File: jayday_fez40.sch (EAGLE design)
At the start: 46 parts, among them IC1 GHI_STM32F40X, IC2 LM1117MP-3.3, IC9 MIC4680-ADJ, U3 MICROSD_MICROSD, X4 DX2R005HN2E700

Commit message: finished layout
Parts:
- renumbered N_M_SENS to M_SENS, P+12V to +12V, P+5V to +5V, P+VCC to VCC, X_LCD_OUT to LCD_OUT
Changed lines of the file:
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@@
 <part name="SUPPLY8" library="supply2" deviceset="+5V" device=""/>
 <part name="U$2" library="SparkFun-Connectors" deviceset="RJ45-8" device="PTH"/>
-<part name="X_LCD_OUT" library="ozlollc" deviceset="SHF105" device=""/>
+<part name="LCD_OUT" library="ozlollc" deviceset="SHF105" device=""/>
 <part name="N_M_HEAT" library="ozlollc" deviceset="SI2312BDS" device=""/>
-<part name="N_M_SENS" library="ozlollc" deviceset="SI2312BDS" device=""/>
+<part name="M_SENS" library="ozlollc" deviceset="SI2312BDS" device=""/>
 <part name="SIM900-EXT" library="SparkFun-Connectors" deviceset="M08" device="1X08"/>
 <part name="GND3" library="supply1" deviceset="GND" device=""/>
 <part name="SUPPLY9" library="supply2" deviceset="+12V" device=""/>
 <part name="GND7" library="supply1" deviceset="GND" device=""/>
-<part name="P+5V" library="led" deviceset="LED" device="CHIPLED_0805"/>
+<part name="+5V" library="led" deviceset="LED" device="CHIPLED_0805"/>
 <part name="R7" library="rcl" deviceset="R-US_" device="R0603" value="330"/>
 <part name="V1" library="supply2" deviceset="+5V" device=""/>
 <part name="GND10" library="supply1" deviceset="GND" device=""/>
-<part name="P+VCC" library="led" deviceset="LED" device="CHIPLED_0805"/>
+<part name="VCC" library="led" deviceset="LED" device="CHIPLED_0805"/>
 <part name="R8" library="rcl" deviceset="R-US_" device="R0603" value="330"/>
 <part name="GND11" library="supply1" deviceset="GND" device=""/>
-<part name="P+12V" library="led" deviceset="LED" device="CHIPLED_0805"/>
+<part name="+12V" library="led" deviceset="LED" device="CHIPLED_0805"/>
 <part name="R9" library="rcl" deviceset="R-US_" device="R0603" value="330"/>
 <part name="SUPPLY10" library="supply2" deviceset="+12V" device=""/>
@@
 <instance part="SUPPLY8" gate="+5V" x="111.76" y="116.84" rot="R180"/>
 <instance part="U$2" gate="G$1" x="162.56" y="124.46"/>
-<instance part="X_LCD_OUT" gate="X" x="22.86" y="104.14"/>
+<instance part="LCD_OUT" gate="X" x="22.86" y="104.14"/>
 <instance part="N_M_HEAT" gate="G$1" x="106.68" y="165.1"/>
-<instance part="N_M_SENS" gate="G$1" x="187.96" y="165.1"/>
+<instance part="M_SENS" gate="G$1" x="187.96" y="165.1"/>
 <instance part="SIM900-EXT" gate="G$1" x="243.84" y="121.92"/>
 <instance part="GND3" gate="1" x="261.62" y="106.68"/>
 <instance part="SUPPLY9" gate="+12V" x="256.54" y="106.68" rot="R180"/>
 <instance part="GND7" gate="1" x="203.2" y="-17.78"/>
-<instance part="P+5V" gate="G$1" x="203.2" y="-7.62"/>
+<instance part="+5V" gate="G$1" x="203.2" y="-7.62"/>
 <instance part="R7" gate="G$1" x="203.2" y="2.54" rot="R90"/>
 <instance part="V1" gate="+5V" x="203.2" y="12.7"/>
 <instance part="GND10" gate="1" x="213.36" y="-17.78"/>
-<instance part="P+VCC" gate="G$1" x="213.36" y="-7.62"/>
+<instance part="VCC" gate="G$1" x="213.36" y="-7.62"/>
 <instance part="R8" gate="G$1" x="213.36" y="2.54" rot="R90"/>
 <instance part="GND11" gate="1" x="193.04" y="-17.78"/>
-<instance part="P+12V" gate="G$1" x="193.04" y="-7.62"/>
+<instance part="+12V" gate="G$1" x="193.04" y="-7.62"/>
 <instance part="R9" gate="G$1" x="193.04" y="2.54" rot="R90"/>
 <instance part="SUPPLY10" gate="+12V" x="193.04" y="12.7"/>
@@
 </segment>
 <segment>
-<pinref part="P+5V" gate="G$1" pin="C"/>
+<pinref part="+5V" gate="G$1" pin="C"/>
 <pinref part="GND7" gate="1" pin="GND"/>
 <wire x1="203.2" y1="-12.7" x2="203.2" y2="-15.24" width="0.1524" layer="91"/>
 </segment>
 <segment>
-<pinref part="P+VCC" gate="G$1" pin="C"/>
+<pinref part="VCC" gate="G$1" pin="C"/>
 <pinref part="GND10" gate="1" pin="GND"/>
 <wire x1="213.36" y1="-12.7" x2="213.36" y2="-15.24" width="0.1524" layer="91"/>
 </segment>
 <segment>
-<pinref part="P+12V" gate="G$1" pin="C"/>
+<pinref part="+12V" gate="G$1" pin="C"/>
 <pinref part="GND11" gate="1" pin="GND"/>
 <wire x1="193.04" y1="-12.7" x2="193.04" y2="-15.24" width="0.1524" layer="91"/>
@@
 <wire x1="185.42" y1="149.86" x2="187.96" y2="149.86" width="0.1524" layer="91"/>
 <junction x="187.96" y="149.86"/>
-<pinref part="N_M_SENS" gate="G$1" pin="S"/>
+<pinref part="M_SENS" gate="G$1" pin="S"/>
 <pinref part="R11" gate="G$1" pin="1"/>
 <wire x1="172.72" y1="152.4" x2="172.72" y2="149.86" width="0.1524" layer="91"/>
@@
 <segment>
 <pinref part="SUPPLY15" gate="G$1" pin="VCC"/>
-<pinref part="X_LCD_OUT" gate="X" pin="1"/>
+<pinref part="LCD_OUT" gate="X" pin="1"/>
 </segment>
 <segment>
@@
 </segment>
 <segment>
-<pinref part="X_LCD_OUT" gate="X" pin="2"/>
+<pinref part="LCD_OUT" gate="X" pin="2"/>
 <pinref part="SUPPLY13" gate="+5V" pin="+5V"/>
 </segment>
@@
 </segment>
 <segment>
-<pinref part="X_LCD_OUT" gate="X" pin="6"/>
+<pinref part="LCD_OUT" gate="X" pin="6"/>
 <wire x1="33.02" y1="104.14" x2="58.42" y2="104.14" width="0.1524" layer="91"/>
 <label x="35.56" y="104.14" size="1.778" layer="95"/>
@@
 </segment>
 <segment>
-<pinref part="X_LCD_OUT" gate="X" pin="8"/>
+<pinref part="LCD_OUT" gate="X" pin="8"/>
 <wire x1="33.02" y1="101.6" x2="55.88" y2="101.6" width="0.1524" layer="91"/>
 <wire x1="55.88" y1="101.6" x2="58.42" y2="101.6" width="0.1524" layer="91"/>
@@
 </segment>
 <segment>
-<pinref part="X_LCD_OUT" gate="X" pin="7"/>
+<pinref part="LCD_OUT" gate="X" pin="7"/>
 <wire x1="12.7" y1="101.6" x2="-17.78" y2="101.6" width="0.1524" layer="91"/>
 <label x="-22.86" y="101.6" size="1.778" layer="95"/>
@@
 </segment>
 <segment>
-<pinref part="X_LCD_OUT" gate="X" pin="9"/>
+<pinref part="LCD_OUT" gate="X" pin="9"/>
 <wire x1="12.7" y1="99.06" x2="-17.78" y2="99.06" width="0.1524" layer="91"/>
 <label x="-22.86" y="99.06" size="1.778" layer="95"/>
@@
 </segment>
 <segment>
-<pinref part="X_LCD_OUT" gate="X" pin="5"/>
+<pinref part="LCD_OUT" gate="X" pin="5"/>
 <wire x1="12.7" y1="104.14" x2="-17.78" y2="104.14" width="0.1524" layer="91"/>
 <label x="-22.86" y="104.14" size="1.778" layer="95"/>
@@
 </segment>
 <segment>
-<pinref part="N_M_SENS" gate="G$1" pin="G"/>
+<pinref part="M_SENS" gate="G$1" pin="G"/>
 <wire x1="182.88" y1="162.56" x2="172.72" y2="162.56" width="0.1524" layer="91"/>
 <pinref part="R11" gate="G$1" pin="2"/>
@@
 </segment>
 <segment>
-<pinref part="X_LCD_OUT" gate="X" pin="4"/>
+<pinref part="LCD_OUT" gate="X" pin="4"/>
 <wire x1="33.02" y1="106.68" x2="58.42" y2="106.68" width="0.1524" layer="91"/>
 <label x="35.56" y="106.68" size="1.778" layer="95"/>
@@
 </segment>
 <segment>
-<pinref part="X_LCD_OUT" gate="X" pin="3"/>
+<pinref part="LCD_OUT" gate="X" pin="3"/>
 <wire x1="12.7" y1="106.68" x2="-17.78" y2="106.68" width="0.1524" layer="91"/>
 <label x="-22.86" y="106.68" size="1.778" layer="95"/>
@@
 <wire x1="203.2" y1="-5.08" x2="203.2" y2="-2.54" width="0.1524" layer="91"/>
 <pinref part="R7" gate="G$1" pin="1"/>
-<pinref part="P+5V" gate="G$1" pin="A"/>
+<pinref part="+5V" gate="G$1" pin="A"/>
 </segment>
 </net>
@@
 <wire x1="213.36" y1="-5.08" x2="213.36" y2="-2.54" width="0.1524" layer="91"/>
 <pinref part="R8" gate="G$1" pin="1"/>
-<pinref part="P+VCC" gate="G$1" pin="A"/>
+<pinref part="VCC" gate="G$1" pin="A"/>
 </segment>
 </net>
@@
 <wire x1="193.04" y1="-5.08" x2="193.04" y2="-2.54" width="0.1524" layer="91"/>
 <pinref part="R9" gate="G$1" pin="1"/>
-<pinref part="P+12V" gate="G$1" pin="A"/>
+<pinref part="+12V" gate="G$1" pin="A"/>
 </segment>
 </net>
@@
 <net name="SENS_OUT" class="0">
 <segment>
-<pinref part="N_M_SENS" gate="G$1" pin="D"/>
+<pinref part="M_SENS" gate="G$1" pin="D"/>
 <wire x1="187.96" y1="170.18" x2="187.96" y2="172.72" width="0.1524" layer="91"/>
 <wire x1="187.96" y1="172.72" x2="147.32" y2="172.72" width="0.1524" layer="91"/>
@@
 </segment>
 <segment>
-<pinref part="X_LCD_OUT" gate="X" pin="10"/>
+<pinref part="LCD_OUT" gate="X" pin="10"/>
 <wire x1="33.02" y1="99.06" x2="58.42" y2="99.06" width="0.1524" layer="91"/>
 <label x="35.56" y="99.06" size="1.778" layer="95"/>

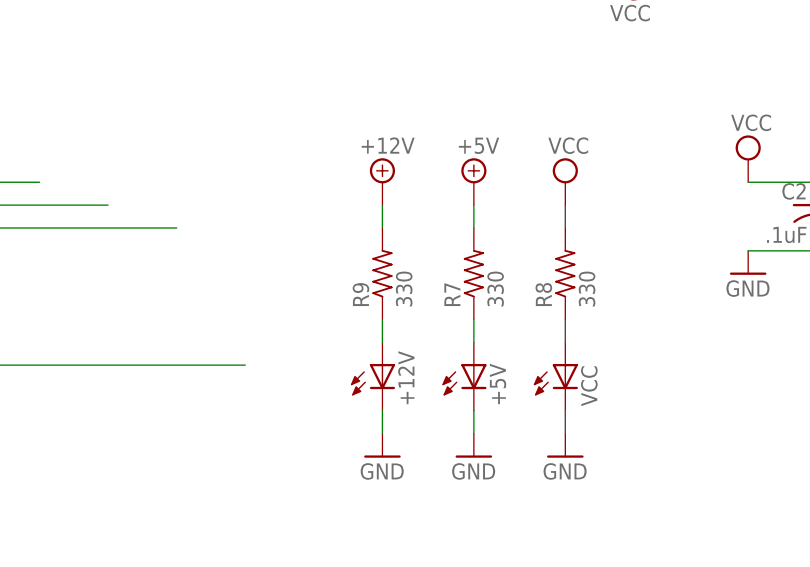
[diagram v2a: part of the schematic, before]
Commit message: fixed R9 to 825ohms
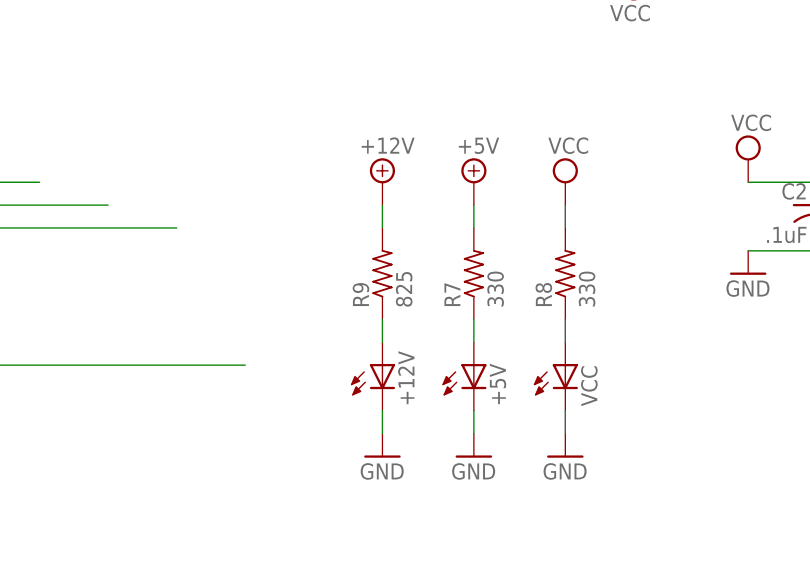
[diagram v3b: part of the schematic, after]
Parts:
- R9: value 330 -> 825
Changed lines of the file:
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@@
 <part name="GND11" library="supply1" deviceset="GND" device=""/>
 <part name="+12V" library="led" deviceset="LED" device="CHIPLED_0805"/>
-<part name="R9" library="rcl" deviceset="R-US_" device="R0603" value="330"/>
+<part name="R9" library="rcl" deviceset="R-US_" device="R0603" value="825"/>
 <part name="SUPPLY10" library="supply2" deviceset="+12V" device=""/>
 <part name="SUPPLY12" library="supply2" deviceset="+12V" device=""/>
